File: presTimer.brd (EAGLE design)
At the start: 34 x 40.6 mm, 9 parts, among them J2 POWER_JACKPTH

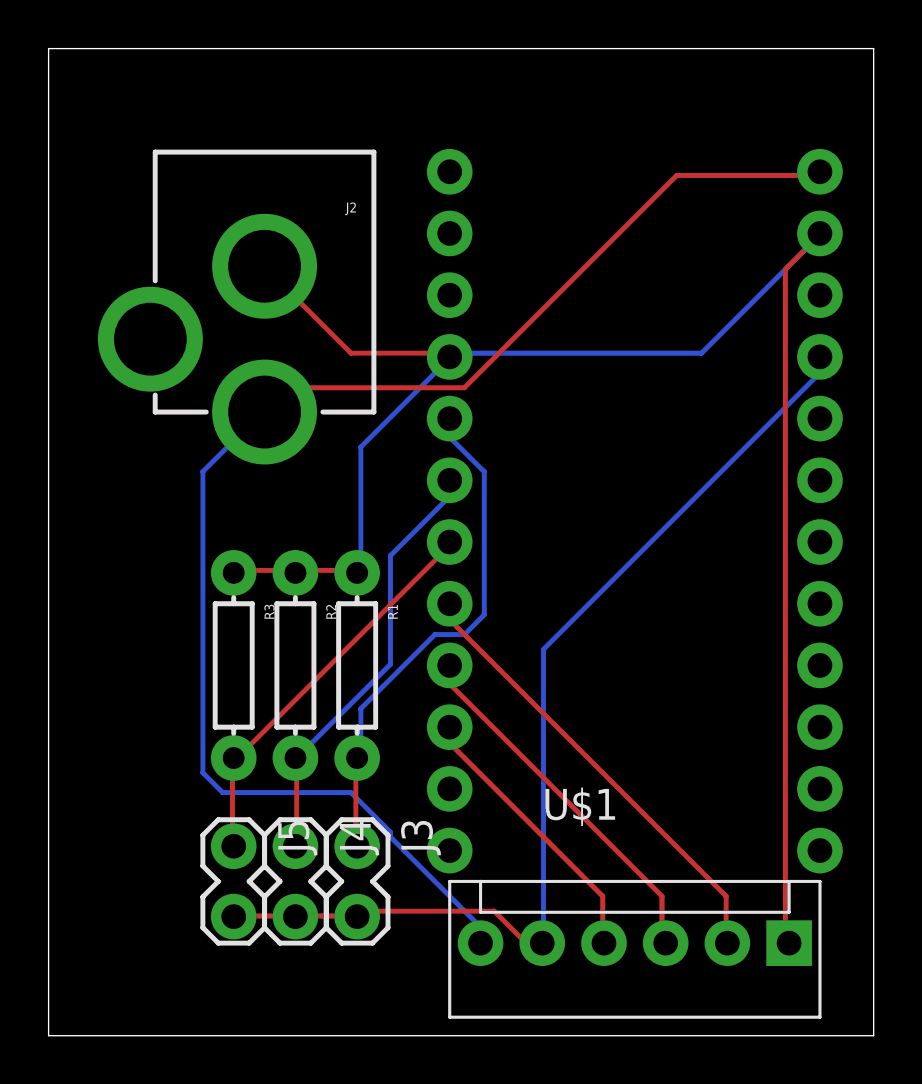
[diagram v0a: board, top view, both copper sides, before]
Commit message: Updated circuit board layout
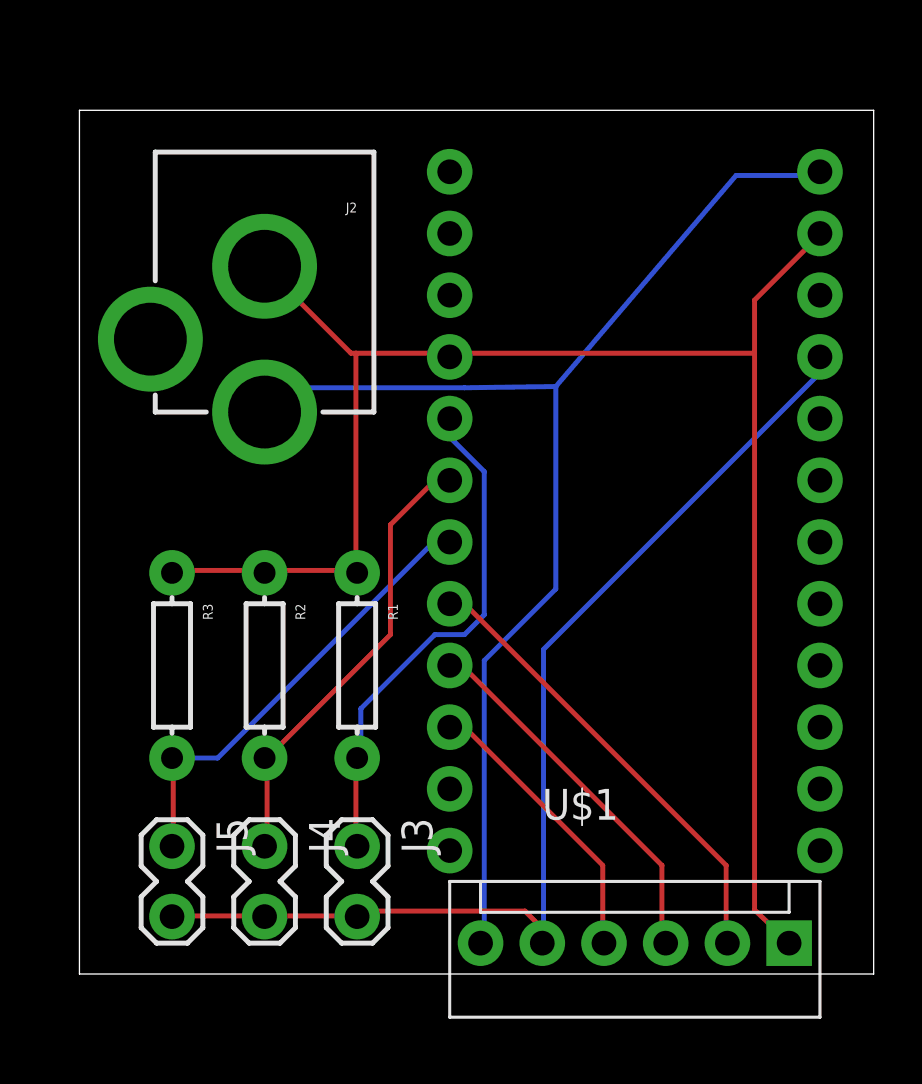
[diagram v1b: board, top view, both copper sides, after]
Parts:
- moved J5 2.54 mm to (14.0, 11.4)
- moved R3 2.54 mm to (14.0, 19.1)
- moved J4 1.27 mm to (17.8, 11.4)
- moved R2 1.27 mm to (17.8, 19.1)
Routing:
- net N$5: track 57.9 -> 51.7 mm
- net N$6: track 42.2 -> 46.1 mm
- net GND: track 72.4 -> 69.5 mm
- net N$2: track 16.4 -> 18.9 mm
- net N$3: track 17.8 -> 19.5 mm
- net N$1: track 18.7 -> 19.9 mm
- net N$8: track 11.5 -> 12.7 mm
- net N$7: track 15.1 -> 16.1 mm
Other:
- board size 34 x 40.6 mm -> 32.7 x 35.5 mm
- board text added: "12v"
- board text added: "2"
- board text added: "gnd"
- board text removed: "B2"
